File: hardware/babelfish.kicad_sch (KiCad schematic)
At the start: 90 parts, among them J1 Shifter Power, J2 SWD, J3 DE9 Female, J4 USB_A, Q1 BSS138, SW1 TS342A2P-WZ, SW2 TS342A2P-WZ, SW3 SK12D07VG5_C3020419, U1 RP2040, U10 74HC4052PW,118, U11 MAX3232IDR, U12 AP2191WG-7, U2 TPS2113ADRBR, U3 GT-USB-7010ASV, U4 W25Q128JVS, U5 TPMCP1703T-5002E_CB, U6 TPMCP1703T-3302E_CB, U7 74HC4052PW,118, U8 74HC4052PW,118, U9 74HC4052PW,118, X1 X322512MSB4SI

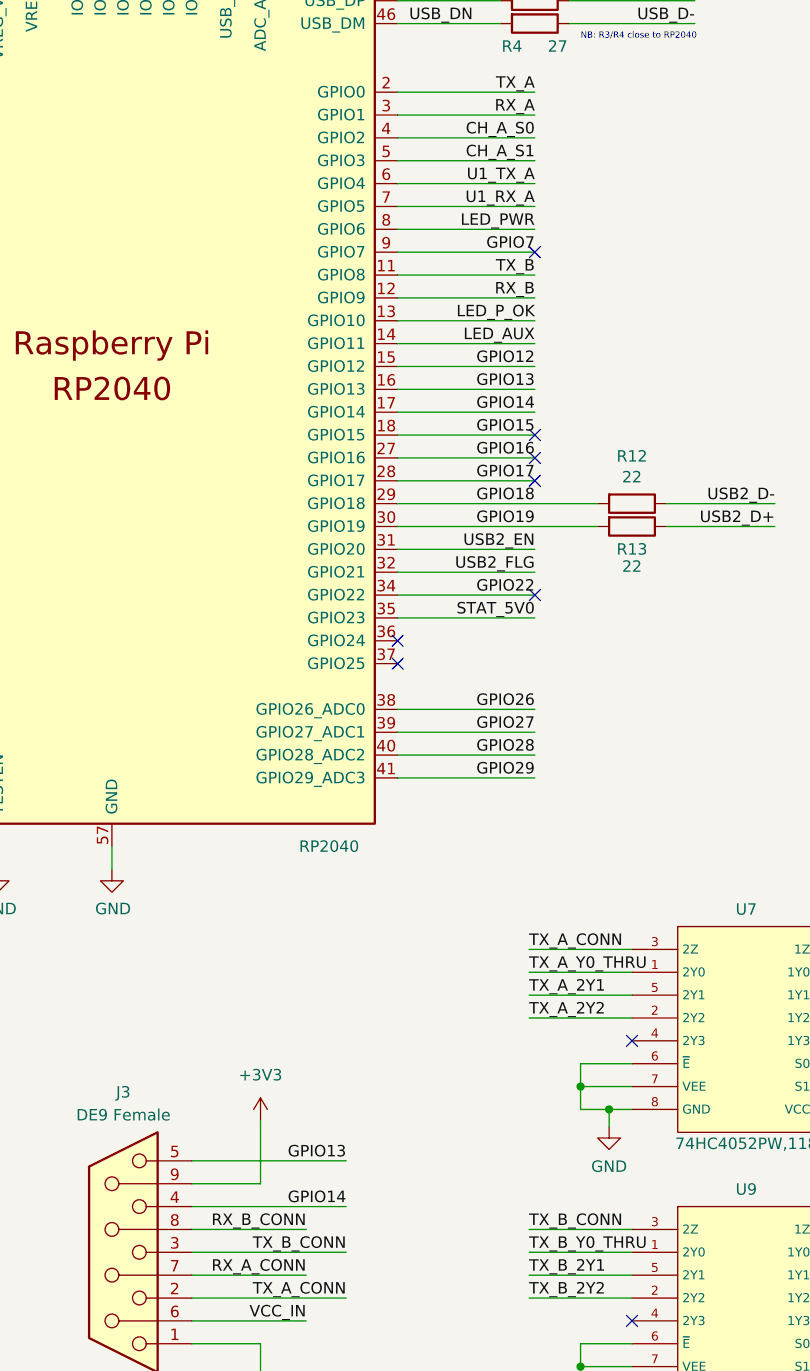
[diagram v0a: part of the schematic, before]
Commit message: Er, forgot to wire CH_B_S0/1
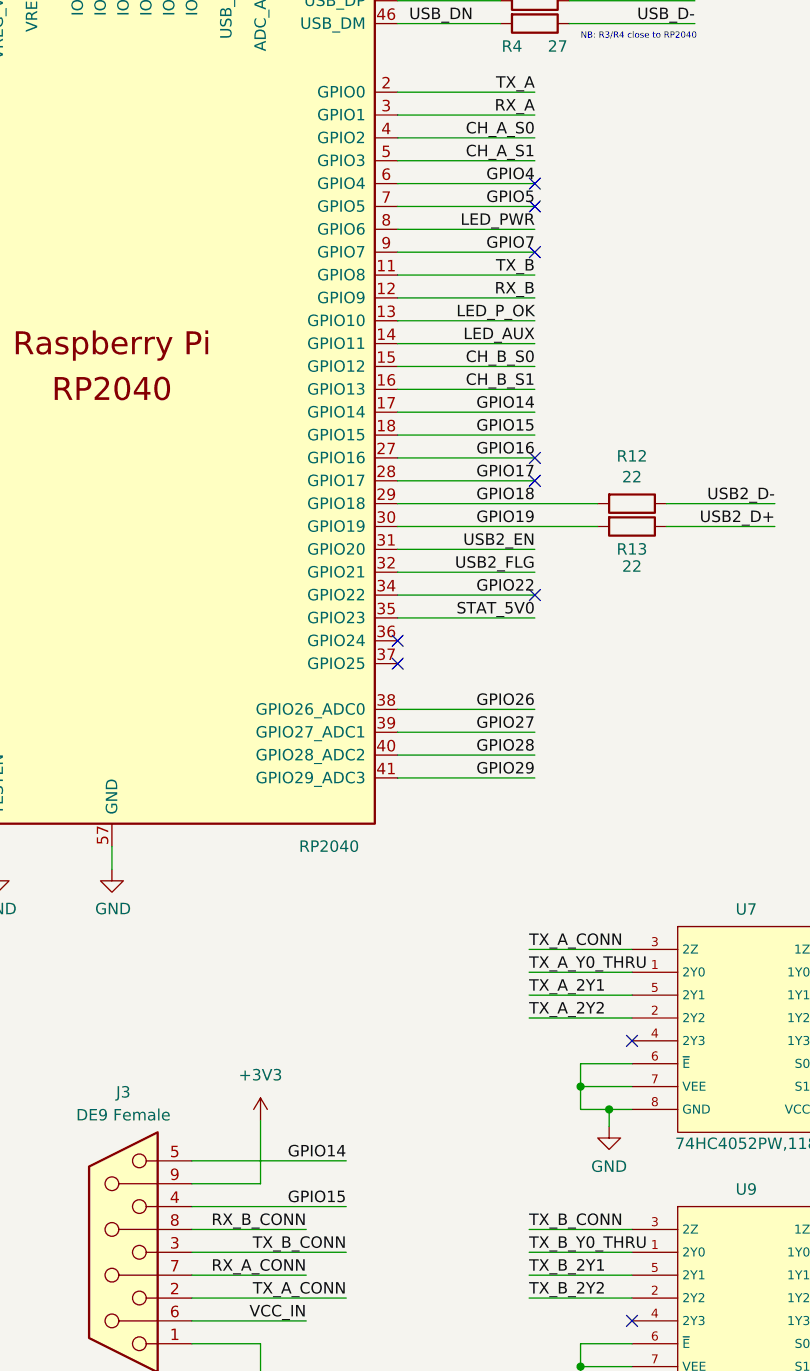
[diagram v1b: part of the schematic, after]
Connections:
- net GPIO12 is gone; now on net CH_B_S0: U1.15 (GPIO12)
- net CH_B_S1: now also U1.16 (GPIO13)
- net GPIO14: now also J3.5; no longer J3.4
- net GPIO15: now also J3.4
- removed net GPIO13: J3.5, U1.16 (GPIO13)
- net U1_RX_A renamed GPIO5
- net U1_TX_A renamed GPIO4
- no-connect marks 15 -> 16
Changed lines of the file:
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@@
   (no_connect (at 187.325 125.095))
   (no_connect (at 198.12 187.325))
-  (no_connect (at 187.325 120.015))
   (no_connect (at 223.52 187.325))
   (no_connect (at 187.325 99.695))
   (no_connect (at 172.085 142.875))
+  (no_connect (at 187.325 92.075))
+  (no_connect (at 187.325 94.615))
   (no_connect (at 267.97 187.325))
   (no_connect (at 223.52 218.44))
@@
     (effects (font (size 1.27 1.27)) (justify left bottom))
   )
-  (label "GPIO13" (at 166.37 200.66 180) (fields_autoplaced)
+  (label "GPIO14" (at 166.37 200.66 180) (fields_autoplaced)
     (effects (font (size 1.27 1.27)) (justify right bottom))
   )
@@
     (effects (font (size 1.27 1.27)) (justify left bottom))
   )
-  (label "GPIO14" (at 166.37 205.74 180) (fields_autoplaced)
+  (label "GPIO15" (at 166.37 205.74 180) (fields_autoplaced)
     (effects (font (size 1.27 1.27)) (justify right bottom))
   )
@@
     (effects (font (size 1.27 1.27)) (justify left bottom))
   )
-  (label "U1_RX_A" (at 187.325 94.615 180) (fields_autoplaced)
+  (label "GPIO5" (at 187.325 94.615 180) (fields_autoplaced)
     (effects (font (size 1.27 1.27)) (justify right bottom))
   )
@@
     (effects (font (size 1.27 1.27)) (justify right bottom))
   )
-  (label "GPIO12" (at 187.325 112.395 180) (fields_autoplaced)
+  (label "CH_B_S0" (at 187.325 112.395 180) (fields_autoplaced)
     (effects (font (size 1.27 1.27)) (justify right bottom))
   )
@@
     (effects (font (size 1.27 1.27)) (justify right bottom))
   )
-  (label "U1_TX_A" (at 187.325 92.075 180) (fields_autoplaced)
+  (label "GPIO4" (at 187.325 92.075 180) (fields_autoplaced)
     (effects (font (size 1.27 1.27)) (justify right bottom))
   )
@@
     (effects (font (size 1.27 1.27)) (justify right bottom))
   )
-  (label "GPIO13" (at 187.325 114.935 180) (fields_autoplaced)
-    (effects (font (size 1.27 1.27)) (justify right bottom))
-  )
+  (label "CH_B_S1" (at 187.325 114.935 180) (fields_autoplaced)
+    (effects (font (size 1.27 1.27)) (justify right bottom))
+  )

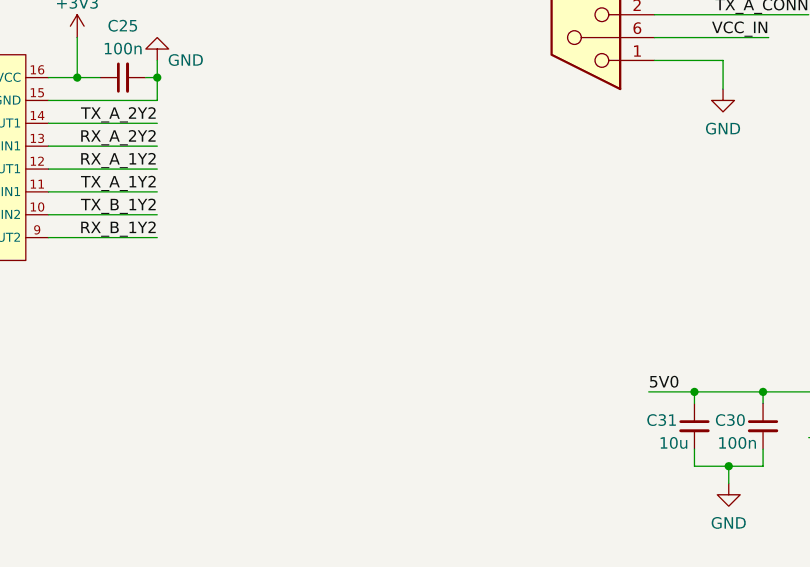
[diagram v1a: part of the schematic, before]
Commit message: hw: Add back test points to schematic, fix db9 GND
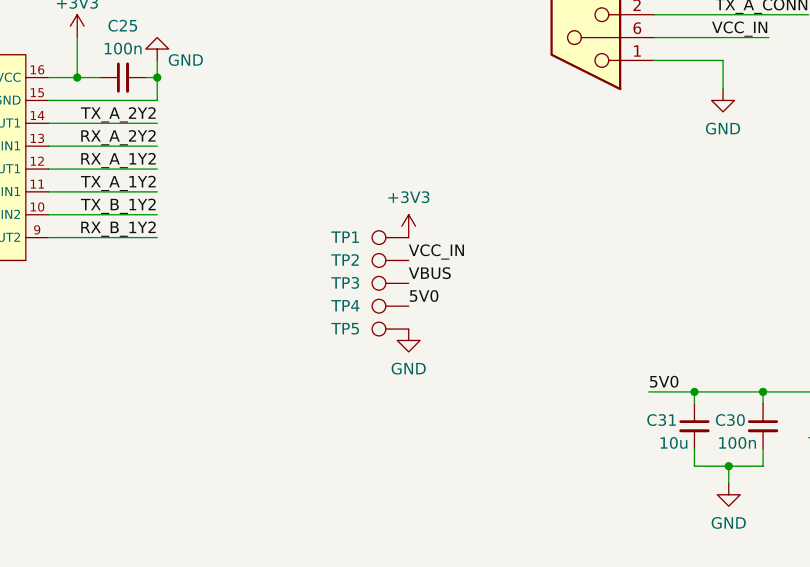
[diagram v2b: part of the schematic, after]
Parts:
- added TP1, TP2, TP3, TP4, TP5: TestPoint, TestPoint:TestPoint_Pad_D1.0mm, symbol Connector:TestPoint
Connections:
- net +3V3: now also TP1.1
- net 5V0: now also TP4.1
- net GND: now also TP5.1
- net VBUS: now also TP3.1
- net VCC_IN: now also TP2.1
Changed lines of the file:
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@@
     (effects (font (size 1.27 1.27)) (justify left bottom))
   )
+  (label "VBUS" (at 121.92 245.745 0) (fields_autoplaced)
+    (effects (font (size 1.27 1.27)) (justify left bottom))
+  )
+  (label "5V0" (at 121.92 248.285 0) (fields_autoplaced)
+    (effects (font (size 1.27 1.27)) (justify left bottom))
+  )
   (label "SWCLK" (at 94.615 146.685 0) (fields_autoplaced)
     (effects (font (size 1.27 1.27)) (justify left bottom))
@@
     (effects (font (size 1.27 1.27)) (justify right bottom))
   )
+  (label "VCC_IN" (at 121.92 243.205 0) (fields_autoplaced)
+    (effects (font (size 1.27 1.27)) (justify left bottom))
+  )
   (label "TX_A_2Y2" (at 93.98 227.965 180) (fields_autoplaced)
     (effects (font (size 1.27 1.27)) (justify right bottom))
@@
     )
   )
+  (symbol (lib_id "Connector:TestPoint") (at 121.92 240.665 90) (unit 1)
+    (in_bom yes) (on_board yes) (dnp no)
+    (property "Reference" "TP1" (at 114.935 240.665 90)
+      (effects (font (size 1.27 1.27)))
+    )
+    (property "Value" "TestPoint" (at 118.618 237.49 90)
+      (effects (font (size 1.27 1.27)) hide)
+    )
+    (property "Footprint" "TestPoint:TestPoint_Pad_D1.0mm" (at 121.92 235.585 0)
+      (effects (font (size 1.27 1.27)) hide)
+    )
+    (property "Datasheet" "~" (at 121.92 235.585 0)
+      (effects (font (size 1.27 1.27)) hide)
+    )
+    (pin "1")
+    (instances
+      (project "babelfish"
+        (path "/25a7582e-3999-4fda-9acd-cd1e305548b6"
+          (reference "TP1") (unit 1)
+        )
+      )
+    )
+  )
   (symbol (lib_id "power:GND") (at 67.31 142.875 0) (unit 1)
     (in_bom yes) (on_board yes) (dnp no) (fields_autoplaced)
@@
     )
   )
+  (symbol (lib_id "power:GND") (at 121.92 250.825 0) (unit 1)
+    (in_bom yes) (on_board yes) (dnp no) (fields_autoplaced)
+    (property "Reference" "#PWR063" (at 121.92 257.175 0)
+      (effects (font (size 1.27 1.27)) hide)
+    )
+    (property "Value" "GND" (at 121.92 255.27 0)
+      (effects (font (size 1.27 1.27)))
+    )
+    (property "Footprint" "" (at 121.92 250.825 0)
+      (effects (font (size 1.27 1.27)) hide)
+    )
+    (property "Datasheet" "" (at 121.92 250.825 0)
+      (effects (font (size 1.27 1.27)) hide)
+    )
+    (pin "1")
+    (instances
+      (project "babelfish"
+        (path "/25a7582e-3999-4fda-9acd-cd1e305548b6"
+          (reference "#PWR063") (unit 1)
+        )
+      )
+    )
+  )
   (symbol (lib_id "Device:R_Small") (at 363.22 54.61 270) (mirror x) (unit 1)
     (in_bom yes) (on_board yes) (dnp no)
@@
     )
   )
+  (symbol (lib_id "Connector:TestPoint") (at 121.92 245.745 90) (unit 1)
+    (in_bom yes) (on_board yes) (dnp no)
+    (property "Reference" "TP3" (at 114.935 245.745 90)
+      (effects (font (size 1.27 1.27)))
+    )
+    (property "Value" "TestPoint" (at 118.618 242.57 90)
+      (effects (font (size 1.27 1.27)) hide)
+    )
+    (property "Footprint" "TestPoint:TestPoint_Pad_D1.0mm" (at 121.92 240.665 0)
+      (effects (font (size 1.27 1.27)) hide)
+    )
+    (property "Datasheet" "~" (at 121.92 240.665 0)
+      (effects (font (size 1.27 1.27)) hide)
+    )
+    (pin "1")
+    (instances
+      (project "babelfish"
+        (path "/25a7582e-3999-4fda-9acd-cd1e305548b6"
+          (reference "TP3") (unit 1)
+        )
+      )
+    )
+  )
   (symbol (lib_id "Device:Q_NMOS_GSD") (at 349.25 199.39 270) (unit 1)
     (in_bom yes) (on_board yes) (dnp no)
@@
     )
   )
+  (symbol (lib_id "power:+3V3") (at 121.92 240.665 0) (unit 1)
+    (in_bom yes) (on_board yes) (dnp no) (fields_autoplaced)
+    (property "Reference" "#PWR062" (at 121.92 244.475 0)
+      (effects (font (size 1.27 1.27)) hide)
+    )
+    (property "Value" "+3V3" (at 121.92 236.22 0)
+      (effects (font (size 1.27 1.27)))
+    )
+    (property "Footprint" "" (at 121.92 240.665 0)
+      (effects (font (size 1.27 1.27)) hide)
+    )
+    (property "Datasheet" "" (at 121.92 240.665 0)
+      (effects (font (size 1.27 1.27)) hide)
+    )
+    (pin "1")
+    (instances
+      (project "babelfish"
+        (path "/25a7582e-3999-4fda-9acd-cd1e305548b6"
+          (reference "#PWR062") (unit 1)
+        )
+      )
+    )
+  )
   (symbol (lib_id "LCSC:TS342A2P-WZ") (at 76.835 135.255 0) (unit 1)
     (in_bom yes) (on_board yes) (dnp no)
@@
     )
   )
+  (symbol (lib_id "Connector:TestPoint") (at 121.92 250.825 90) (unit 1)
+    (in_bom yes) (on_board yes) (dnp no)
+    (property "Reference" "TP5" (at 114.935 250.825 90)
+      (effects (font (size 1.27 1.27)))
+    )
+    (property "Value" "TestPoint" (at 118.618 247.65 90)
+      (effects (font (size 1.27 1.27)) hide)
+    )
+    (property "Footprint" "TestPoint:TestPoint_Pad_D1.0mm" (at 121.92 245.745 0)
+      (effects (font (size 1.27 1.27)) hide)
+    )
+    (property "Datasheet" "~" (at 121.92 245.745 0)
+      (effects (font (size 1.27 1.27)) hide)
+    )
+    (pin "1")
+    (instances
+      (project "babelfish"
+        (path "/25a7582e-3999-4fda-9acd-cd1e305548b6"
+          (reference "TP5") (unit 1)
+        )
+      )
+    )
+  )
   (symbol (lib_id "Device:R_Small") (at 340.36 233.68 0) (unit 1)
     (in_bom yes) (on_board yes) (dnp no)
@@
     )
   )
+  (symbol (lib_id "Connector:TestPoint") (at 121.92 248.285 90) (unit 1)
+    (in_bom yes) (on_board yes) (dnp no)
+    (property "Reference" "TP4" (at 114.935 248.285 90)
+      (effects (font (size 1.27 1.27)))
+    )
+    (property "Value" "TestPoint" (at 118.618 245.11 90)
+      (effects (font (size 1.27 1.27)) hide)
+    )
+    (property "Footprint" "TestPoint:TestPoint_Pad_D1.0mm" (at 121.92 243.205 0)
+      (effects (font (size 1.27 1.27)) hide)
+    )
+    (property "Datasheet" "~" (at 121.92 243.205 0)
+      (effects (font (size 1.27 1.27)) hide)
+    )
+    (pin "1")
+    (instances
+      (project "babelfish"
+        (path "/25a7582e-3999-4fda-9acd-cd1e305548b6"
+          (reference "TP4") (unit 1)
+        )
+      )
+    )
+  )
   (symbol (lib_id "power:GND") (at 332.105 55.88 0) (unit 1)
     (in_bom yes) (on_board yes) (dnp no) (fields_autoplaced)
@@
         )
       )
+    )
+  )
+  (symbol (lib_id "Connector:TestPoint") (at 121.92 243.205 90) (unit 1)
+    (in_bom yes) (on_board yes) (dnp no)
+    (property "Reference" "TP2" (at 114.935 243.205 90)
+      (effects (font (size 1.27 1.27)))
+    )
+    (property "Value" "TestPoint" (at 118.618 240.03 90)
+      (effects (font (size 1.27 1.27)) hide)
+    )
+    (property "Footprint" "TestPoint:TestPoint_Pad_D1.0mm" (at 121.92 238.125 0)
+      (effects (font (size 1.27 1.27)) hide)
+    )
+    (property "Datasheet" "~" (at 121.92 238.125 0)
+      (effects (font (size 1.27 1.27)) hide)
+    )
+    (pin "1")
+    (instances
+      (project "babelfish"
+        (path "/25a7582e-3999-4fda-9acd-cd1e305548b6"
+          (reference "TP2") (unit 1)
+        )
+      )
